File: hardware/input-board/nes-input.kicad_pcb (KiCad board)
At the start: 2 copper layers, 101.6 x 38.1 mm, 28 parts, among them J1 Main Board, J2 Touch Pad, SW1 Up, SW2 Down, SW3 Left, SW4 Right, SW5 Select, SW6 Start, SW7 B, SW8 A, U1 TCA8418

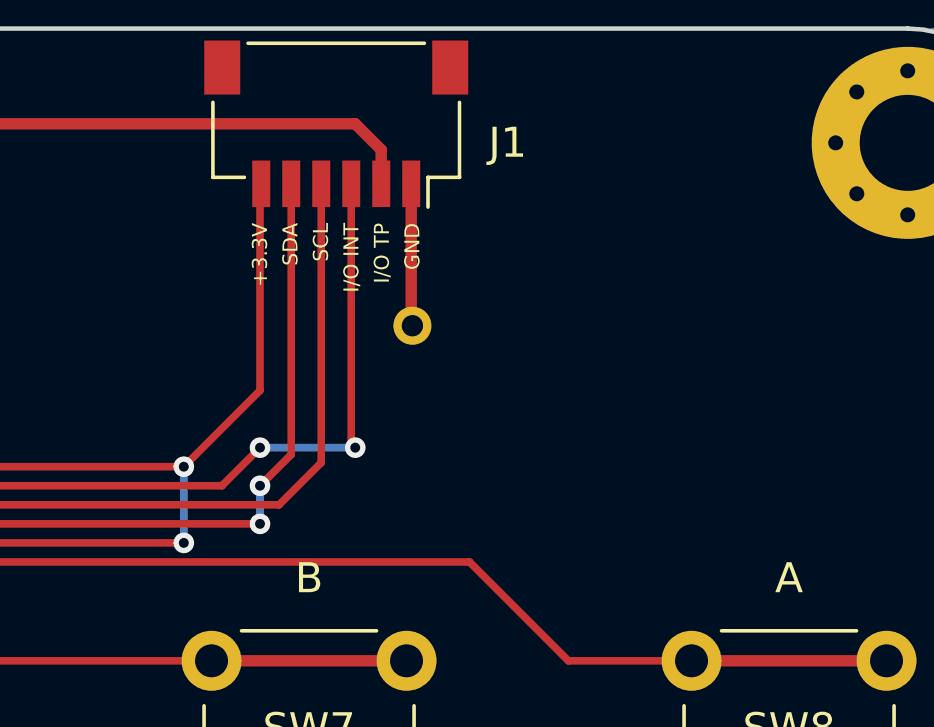
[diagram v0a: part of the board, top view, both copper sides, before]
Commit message: Added TSL2591 component to the input board
The TSL2591 is an ambient light sensor, replacing the TSL250 originally
used on the main board. It is much better at detecting light through the
enclosure.

Added the component symbol, footprint, and approximate 3D model.
Integrated the component into the schematic.
Updated the PCB layout to include the component in the specific location
where the updated enclosure will have light holes.

The footprint should be accurate to the datasheet.
The 3D model is a generic DFN component in the same dimensions as the
TSL2591, but looks nothing like it.

Fixes #10
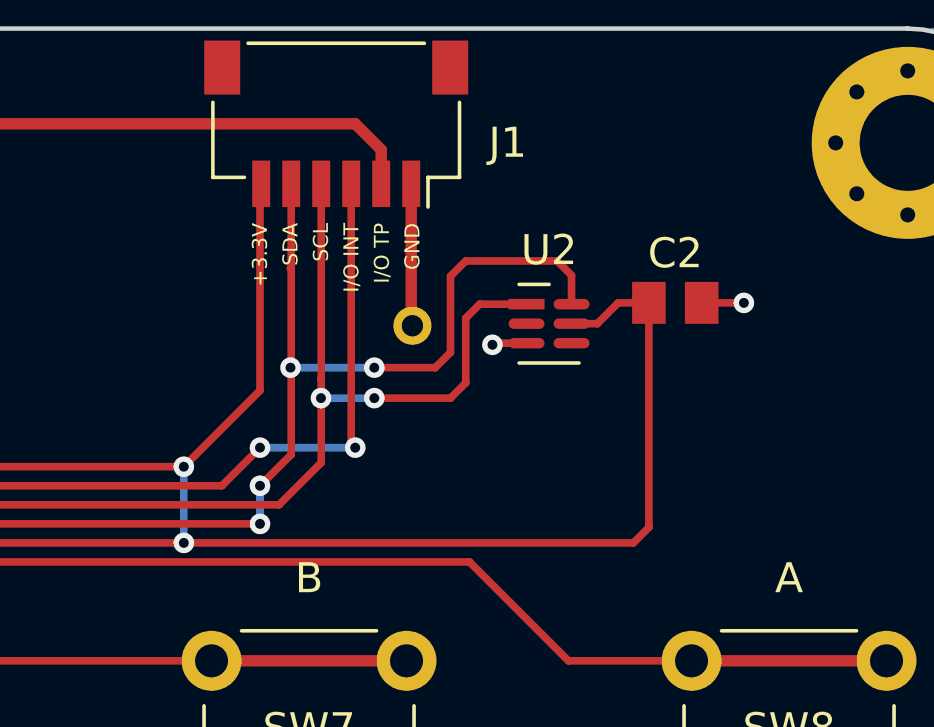
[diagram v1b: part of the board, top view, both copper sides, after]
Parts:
- added C2: 1uF, Capacitor_SMD:C_0805_2012Metric, F.Cu at (140.2, 75.8)
- added U2: TSL2591, lib_fp:AMS_TSL2591, F.Cu at (136.0, 76.5)
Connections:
- U1 pad 25: GND -> (no net)
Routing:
- net +3V3: track 106.3 -> 132.3 mm
- net Net-(J1-Pad5): track 58.6 -> 72.2 mm, vias 2 -> 4
- net Net-(J1-Pad4): track 58.7 -> 68.1 mm, vias 0 -> 2
- net GND: track 11.2 -> 13.7 mm, vias 0 -> 2

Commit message: Add center pad to TCA8418 footprint
This change makes the center pad appear as a grounded pin in the
netlist, and thus makes the PCB's DRC pass without any warnings.

It is not actually a functional change, nor is it actually a change to
any traces in the PCB layout.
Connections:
- U1 pad 25: (no net) -> GND
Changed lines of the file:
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@@
 (kicad_pcb (version 4) (host pcbnew 4.0.7)
   (general
-    (links 64)
+    (links 65)
     (no_connects 0)
     (area 50.089999 66.599999 151.840001 104.850001)
@@
   )
   (setup
-    (last_trace_width 0.254)
+    (last_trace_width 0.1524)
     (user_trace_width 0.254)
     (user_trace_width 0.381)
@@
       (net 4 "Net-(J1-Pad3)"))
     (pad "" smd rect (at 0.64 0.64 270) (size 1.08 1.08) (layers F.Paste))
-    (pad 25 smd rect (at 0 0 270) (size 2.45 2.45) (layers F.Cu F.Mask))
+    (pad 25 smd rect (at 0 0 270) (size 2.45 2.45) (layers F.Cu F.Mask)
+      (net 2 GND))
     (pad "" smd rect (at -0.64 0.64 270) (size 1.08 1.08) (layers F.Paste))
     (pad "" smd rect (at -0.64 -0.64 270) (size 1.08 1.08) (layers F.Paste))

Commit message: Updated schematic and PCB references for Rev B
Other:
- board text added: "Rev: B 2018-07-04"
- board text removed: "Rev: A 2018-04-14"
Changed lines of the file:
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@@
   (title_block
     (title "Nestronic Input Board")
-    (date 2018-04-14)
-    (rev A)
+    (date 2018-07-04)
+    (rev B)
     (company LogicProbe.org)
     (comment 1 "Derek Konigsberg")
@@
   (gr_line (start 62.23 99.06) (end 73.66 99.06) (angle 90) (layer B.SilkS) (width 0.2))
   (gr_line (start 62.23 102.87) (end 62.23 99.06) (angle 90) (layer B.SilkS) (width 0.2))
-  (gr_text "Rev: A\n2018-04-14" (at 73.025 100.965) (layer B.SilkS)
+  (gr_text "Rev: B\n2018-07-04" (at 73.025 100.965) (layer B.SilkS)
     (effects (font (size 1 1) (thickness 0.15)) (justify left mirror))
   )
